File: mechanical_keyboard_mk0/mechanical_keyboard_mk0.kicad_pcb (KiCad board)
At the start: 2 copper layers, 55.9 x 55.9 mm, 8 parts, among them SW1 SW_SPST, SW2 SW_SPST, SW3 SW_SPST, SW4 SW_SPST

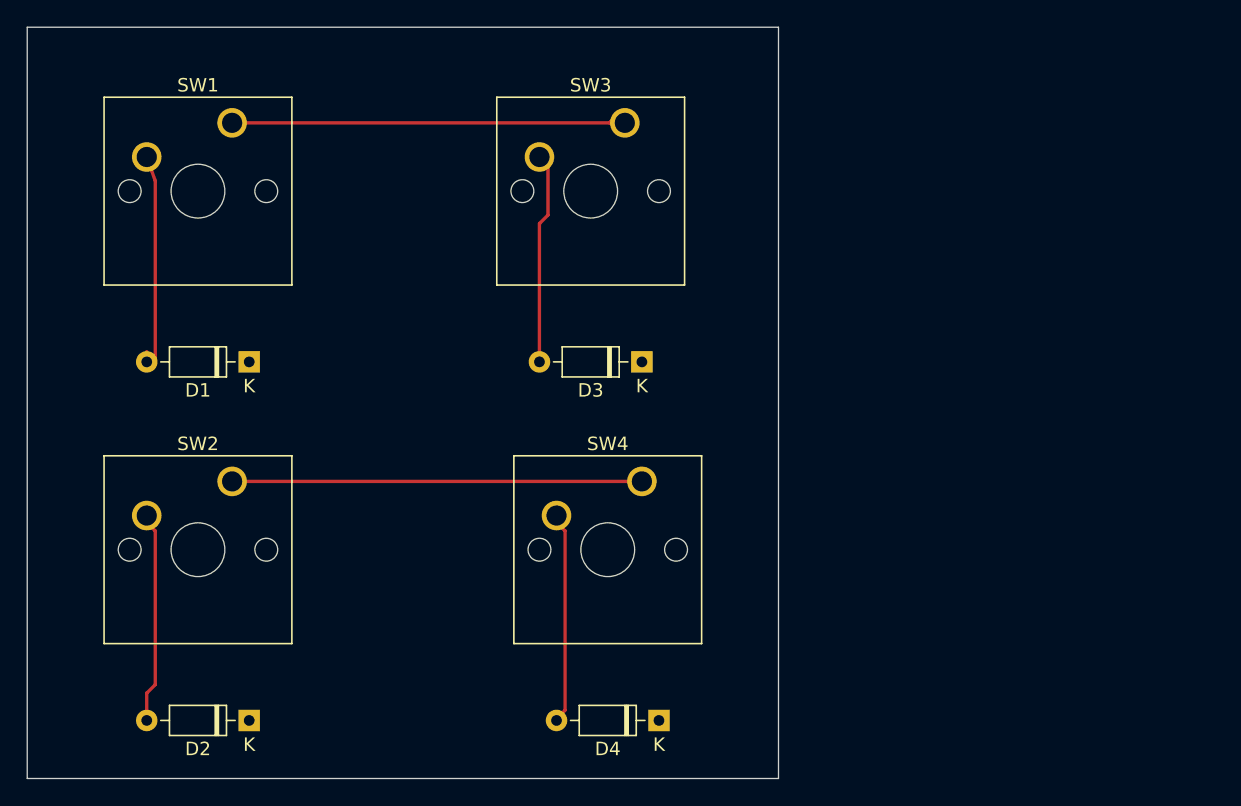
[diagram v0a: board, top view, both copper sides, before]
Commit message: Updated layout, created first output job.
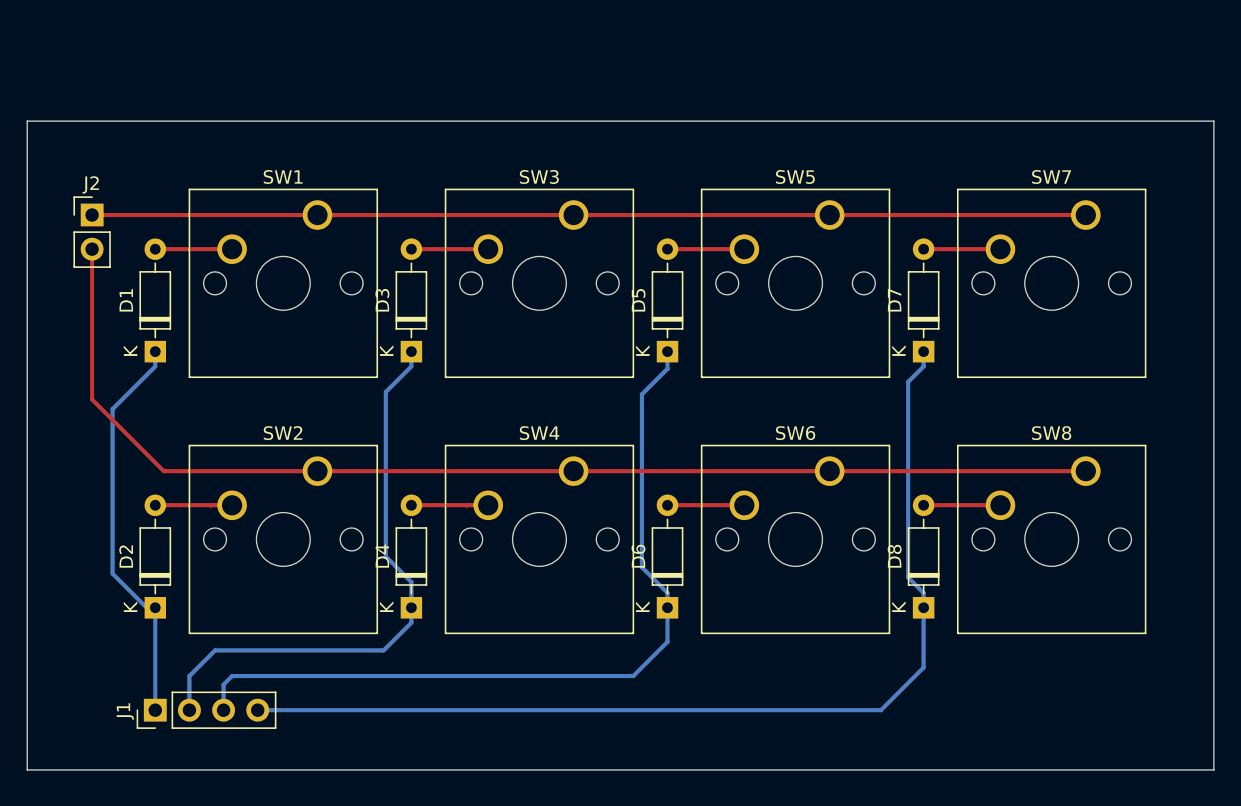
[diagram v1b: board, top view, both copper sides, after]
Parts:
- added D5: 1N4148, Diode_THT:D_DO-35_SOD27_P7.62mm_Horizontal, F.Cu at (139.1, 58.9)
- added D6: 1N4148, Diode_THT:D_DO-35_SOD27_P7.62mm_Horizontal, F.Cu at (139.1, 78.0)
- added D7: 1N4148, Diode_THT:D_DO-35_SOD27_P7.62mm_Horizontal, F.Cu at (158.1, 58.9)
- added D8: 1N4148, Diode_THT:D_DO-35_SOD27_P7.62mm_Horizontal, F.Cu at (158.1, 78.0)
- added J1: Conn_01x04, Connector_PinHeader_2.54mm:PinHeader_1x04_P2.54mm_Vertical, F.Cu at (101.0, 85.6)
- added J2: Conn_01x02, Connector_PinHeader_2.54mm:PinHeader_1x02_P2.54mm_Vertical, F.Cu at (96.3, 48.8)
- added SW5: SW_SPST, Button_Switch_Keyboard:SW_Cherry_MX_1.00u_PCB, F.Cu at (151.1, 48.8)
- added SW6: SW_SPST, Button_Switch_Keyboard:SW_Cherry_MX_1.00u_PCB, F.Cu at (151.1, 67.8)
- added SW7: SW_SPST, Button_Switch_Keyboard:SW_Cherry_MX_1.00u_PCB, F.Cu at (170.2, 48.8)
- added SW8: SW_SPST, Button_Switch_Keyboard:SW_Cherry_MX_1.00u_PCB, F.Cu at (170.2, 67.8)
- moved D4 20.2 mm to (120.0, 78.0), turned to 90 degrees
- moved D3 17.2 mm to (120.0, 58.9), turned to 90 degrees
- moved D2 10.9 mm to (101.0, 78.0), turned to 90 degrees
- moved SW1 9.35 mm to (113.0, 48.8)
- moved SW3 7.85 mm to (132.1, 48.8)
- moved D1 7.03 mm to (101.0, 58.9), turned to 90 degrees
- moved SW2 6.40 mm to (113.0, 67.8)
- moved SW4 5.14 mm to (132.1, 67.8)
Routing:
- net /key_matrix/col_3: track 0.00 -> 75.3 mm
- net /key_matrix/col_2: track 0.00 -> 59.4 mm
- net /key_matrix/row_1: track 31.2 -> 86.7 mm
- net /key_matrix/row_0: track 29.3 -> 74.5 mm
- net /key_matrix/col_1: track 0.00 -> 42.4 mm
- net /key_matrix/col_0: track 0.00 -> 29.0 mm
- net Net-(D1-Pad2): track 16.5 -> 5.72 mm
- net Net-(D3-Pad2): track 15.6 -> 5.72 mm
- net Net-(D2-Pad2): track 15.6 -> 5.72 mm
- net Net-(D4-Pad2): track 15.6 -> 5.72 mm
- net Net-(D8-Pad2): track 0.00 -> 5.72 mm
- net Net-(D7-Pad2): track 0.00 -> 5.72 mm
- net Net-(D6-Pad2): track 0.00 -> 5.72 mm
- net Net-(D5-Pad2): track 0.00 -> 5.72 mm
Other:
- board size 55.9 x 55.9 mm -> 88.3 x 48.3 mm
